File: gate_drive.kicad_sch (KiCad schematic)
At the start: 196 parts, among them J19 Conn_01x03, J20 Conn_01x03, Q1 Q_PNP_BEC, Q2 Q_PNP_BEC, Q3 Q_PNP_BEC, Q4 Q_PNP_BEC, Q5 Q_PNP_BEC, Q6 Q_PNP_BEC, U1 EG3113, U14 INA240A1D, U2 EG3113, U20 INA240A1D, U21 INA240A1D, U4 EG3113, U44 INA240A1D, U5 EG3113, U7 EG3113, U8 EG3113

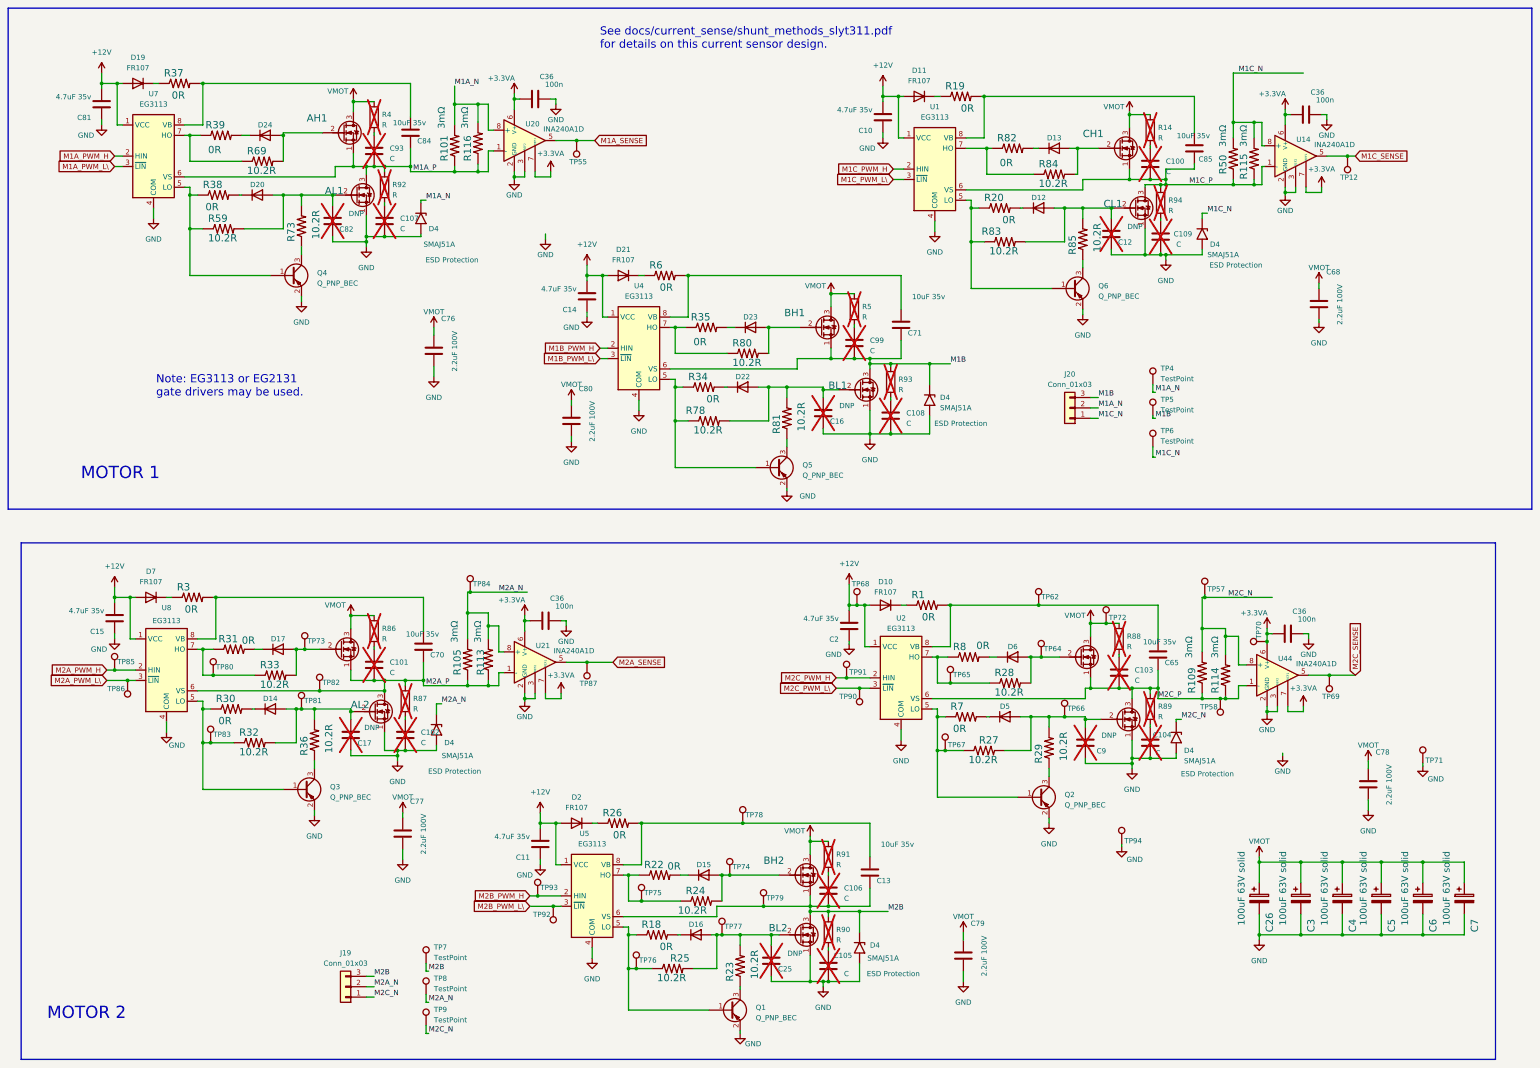
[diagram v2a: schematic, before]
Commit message: Updated board design ready for final design review before fabrication.
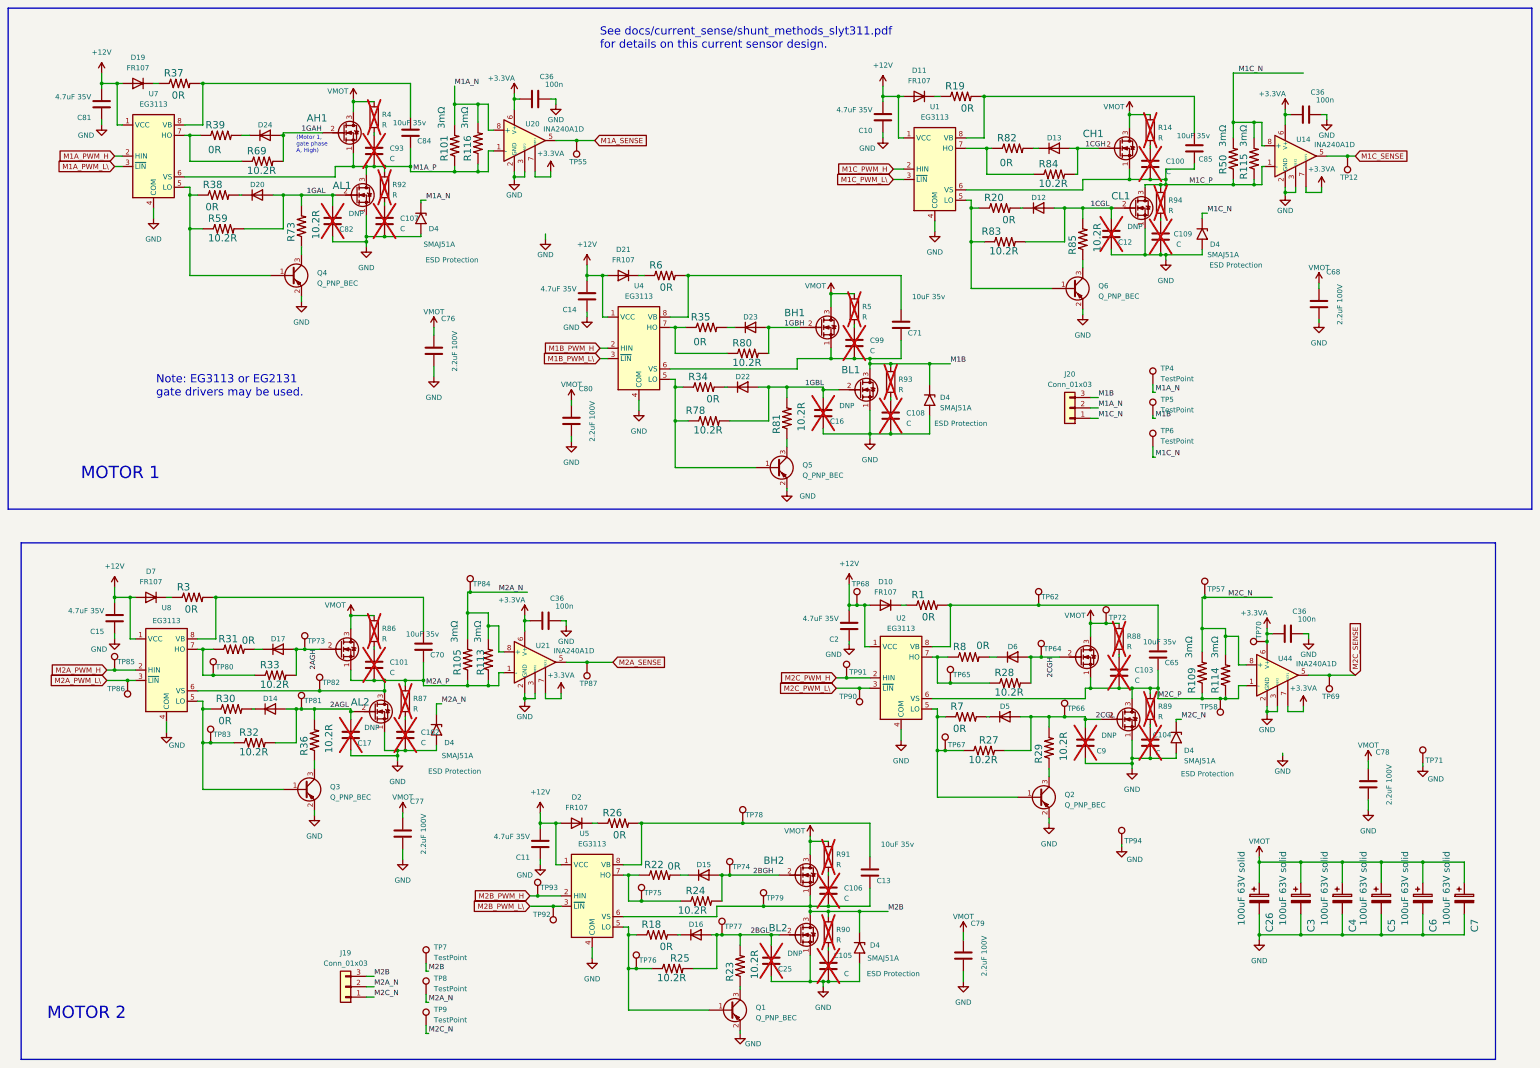
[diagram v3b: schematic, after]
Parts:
- C10, C11, C14, C15, C2, C81: value 4.7uF 35v -> 4.7uF 35V
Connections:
- net 1GAH: now reaches AH1.2 (G), D24.2 (A), R69.2
- net 2CGL: now reaches C9.2, CL2.2 (G), D5.2 (A), R27.2, R29.2, TP66.1
- net 2AGH: now reaches AH2.2 (G), D17.2 (A), R33.2, TP73.1
- net 1GBH: now reaches BH1.2 (G), D23.2 (A), R80.2
- net 2BGH: now reaches BH2.2 (G), D15.2 (A), R24.2, TP74.1
- net 1CGH: now reaches CH1.2 (G), D13.2 (A), R84.2
- net 2BGL: now reaches BL2.2 (G), C25.2, D16.2 (A), R23.2, R25.2, TP77.1
- net 1GBL: now reaches BL1.2 (G), C16.2, D22.2 (A), R78.2, R81.2
- net 1GAL: now reaches AL1.2 (G), C82.2, D20.2 (A), R59.2, R73.2
- net 2CGH: now reaches CH2.2 (G), D6.2 (A), R28.2, TP64.1
- net 2AGL: now reaches AL2.2 (G), C17.2, D14.2 (A), R32.2, R36.2, TP81.1
- net 1CGL: now reaches C12.2, CL1.2 (G), D12.2 (A), R83.2, R85.2
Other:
- note added: "(Motor 1, gate phase A, High)"
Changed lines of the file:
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@@
     (effects (font (size 2 2)) (justify left bottom))
   )
+  (text "(Motor 1,\ngate phase\nA, High)" (at 93.345 52.07 0)
+    (effects (font (size 1 1)) (justify left bottom))
+  )
   (text "MOTOR 1" (at 40.64 132.08 0)
     (effects (font (size 3 3)) (justify left bottom))
@@
     (effects (font (size 1.27 1.27)) (justify left bottom))
   )
+  (label "2BGL" (at 204.47 243.205 0) (fields_autoplaced)
+    (effects (font (size 1.27 1.27)) (justify left bottom))
+  )
   (label "M1C_P" (at 311.785 59.69 0) (fields_autoplaced)
     (effects (font (size 1.27 1.27)) (justify left bottom))
   )
+  (label "2AGL" (at 101.6 187.96 0) (fields_autoplaced)
+    (effects (font (size 1.27 1.27)) (justify left bottom))
+  )
   (label "M1C_N" (at 316.23 66.675 0) (fields_autoplaced)
     (effects (font (size 1.27 1.27)) (justify left bottom))
@@
     (effects (font (size 1.27 1.27)) (justify left bottom))
   )
+  (label "1GBL" (at 217.805 109.22 0) (fields_autoplaced)
+    (effects (font (size 1.27 1.27)) (justify left bottom))
+  )
+  (label "2AGH" (at 98.425 173.355 270) (fields_autoplaced)
+    (effects (font (size 1.27 1.27)) (justify right bottom))
+  )
   (label "M1A_N" (at 132.08 35.56 0) (fields_autoplaced)
     (effects (font (size 1.27 1.27)) (justify left bottom))
@@
     (effects (font (size 1.27 1.27)) (justify left bottom))
   )
+  (label "1GAL" (at 95.885 62.23 0) (fields_autoplaced)
+    (effects (font (size 1.27 1.27)) (justify left bottom))
+  )
+  (label "1CGH" (at 286.385 50.8 0) (fields_autoplaced)
+    (effects (font (size 1.27 1.27)) (justify left bottom))
+  )
   (label "M2C_N" (at 125.73 267.335 0) (fields_autoplaced)
     (effects (font (size 1.27 1.27)) (justify left bottom))
@@
     (effects (font (size 1.27 1.27)) (justify left bottom))
   )
+  (label "2CGH" (at 278.765 175.26 270) (fields_autoplaced)
+    (effects (font (size 1.27 1.27)) (justify right bottom))
+  )
   (label "M1A_N" (at 125.095 63.5 0) (fields_autoplaced)
     (effects (font (size 1.27 1.27)) (justify left bottom))
@@
     (effects (font (size 1.27 1.27)) (justify left bottom))
   )
+  (label "1GBH" (at 212.725 94.615 0) (fields_autoplaced)
+    (effects (font (size 1.27 1.27)) (justify left bottom))
+  )
   (label "M2A_P" (at 125.095 182.245 0) (fields_autoplaced)
     (effects (font (size 1.27 1.27)) (justify left bottom))
   )
+  (label "2BGH" (at 205.105 228.6 0) (fields_autoplaced)
+    (effects (font (size 1.27 1.27)) (justify left bottom))
+  )
+  (label "1GAH" (at 94.615 46.99 0) (fields_autoplaced)
+    (effects (font (size 1.27 1.27)) (justify left bottom))
+  )
   (label "M2C_N" (at 321.31 160.655 0) (fields_autoplaced)
     (effects (font (size 1.27 1.27)) (justify left bottom))
@@
     (effects (font (size 1.27 1.27)) (justify left bottom))
   )
+  (label "2CGL" (at 288.925 190.5 0) (fields_autoplaced)
+    (effects (font (size 1.27 1.27)) (justify left bottom))
+  )
+  (label "1CGL" (at 287.655 65.405 0) (fields_autoplaced)
+    (effects (font (size 1.27 1.27)) (justify left bottom))
+  )
   (label "M1C_N" (at 323.85 32.385 0) (fields_autoplaced)
     (effects (font (size 1.27 1.27)) (justify left bottom))
@@
       (effects (font (size 1.27 1.27)) (justify left bottom))
     )
-    (property "Value" "4.7uF 35v" (at 46.355 163.195 0)
+    (property "Value" "4.7uF 35V" (at 46.355 163.195 0)
       (effects (font (size 1.27 1.27)) (justify left bottom))
     )
@@
   (symbol (lib_id "Device:Q_NMOS_SGD") (at 231.14 109.855 0) (unit 1)
     (in_bom yes) (on_board yes) (dnp no)
-    (property "Reference" "BL1" (at 223.52 109.855 0)
+    (property "Reference" "BL1" (at 226.695 106.045 0)
       (effects (font (size 1.778 1.778)) (justify left bottom))
     )
@@
   (symbol (lib_id "Device:Q_NMOS_SGD") (at 107.95 62.23 0) (unit 1)
     (in_bom yes) (on_board yes) (dnp no)
-    (property "Reference" "AL1" (at 100.33 62.23 0)
+    (property "Reference" "AL1" (at 102.235 60.96 0)
       (effects (font (size 1.778 1.778)) (justify left bottom))
     )
@@
       (effects (font (size 1.27 1.27)) (justify left bottom))
     )
-    (property "Value" "4.7uF 35v" (at 161.925 84.455 0)
+    (property "Value" "4.7uF 35V" (at 161.925 84.455 0)
       (effects (font (size 1.27 1.27)) (justify left bottom))
     )
@@
       (effects (font (size 1.27 1.27)) (justify left bottom))
     )
-    (property "Value" "4.7uF 35v" (at 150.495 218.44 0)
+    (property "Value" "4.7uF 35V" (at 150.495 218.44 0)
       (effects (font (size 1.27 1.27)) (justify left bottom))
     )
@@
       (effects (font (size 1.27 1.27)) (justify left bottom))
     )
-    (property "Value" "4.7uF 35v" (at 43.18 37.465 0)
+    (property "Value" "4.7uF 35V" (at 43.18 37.465 0)
       (effects (font (size 1.27 1.27)) (justify left bottom))
     )
@@
   (symbol (lib_id "Device:Q_NMOS_SGD") (at 112.395 188.595 0) (unit 1)
     (in_bom yes) (on_board yes) (dnp no)
-    (property "Reference" "AL2" (at 106.68 187.96 0)
+    (property "Reference" "AL2" (at 106.68 187.325 0)
       (effects (font (size 1.778 1.778)) (justify left bottom))
     )
@@
       (effects (font (size 1.27 1.27)) (justify left bottom))
     )
-    (property "Value" "4.7uF 35v" (at 234.315 40.64 0)
+    (property "Value" "4.7uF 35V" (at 234.315 40.64 0)
       (effects (font (size 1.27 1.27)) (justify left bottom))
     )
@@
       (effects (font (size 1.27 1.27)) (justify left bottom))
     )
-    (property "Value" "4.7uF 35v" (at 226.06 165.1 0)
+    (property "Value" "4.7uF 35V" (at 226.06 165.1 0)
       (effects (font (size 1.27 1.27)) (justify left bottom))
     )
@@
   (symbol (lib_id "Device:Q_NMOS_SGD") (at 298.45 65.405 0) (unit 1)
     (in_bom yes) (on_board yes) (dnp no)
-    (property "Reference" "CL1" (at 290.83 65.405 0)
+    (property "Reference" "CL1" (at 292.735 63.5 0)
       (effects (font (size 1.778 1.778)) (justify left bottom))
     )

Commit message: Rev 3.1 updated files. ordered Nov 2 2023
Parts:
- J19, J20: LCSC C3040682 -> C99176; now in the parts list
- R23, R24, R25, R27, R28, R29, R32, R33, R36, R59, R69, R73, R78, R80, R81, R83, R84, R85: LCSC C22773 -> C2933129
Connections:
- net GND: now also Q1.3 (C), Q2.3 (C), Q3.3 (C), Q4.3 (C), Q5.3 (C), Q6.3 (C); no longer Q1.2 (E), Q2.2 (E), Q3.2 (E), Q4.2 (E), Q5.2 (E), Q6.2 (E)
- net at R23.1: now also Q1.2 (E); no longer Q1.3 (C)
- net at R29.1: now also Q2.2 (E); no longer Q2.3 (C)
- net at R81.1: now also Q5.2 (E); no longer Q5.3 (C)
- net at R36.1: now also Q3.2 (E); no longer Q3.3 (C)
- net at R85.1: now also Q6.2 (E); no longer Q6.3 (C)
- net at R73.1: now also Q4.2 (E); no longer Q4.3 (C)

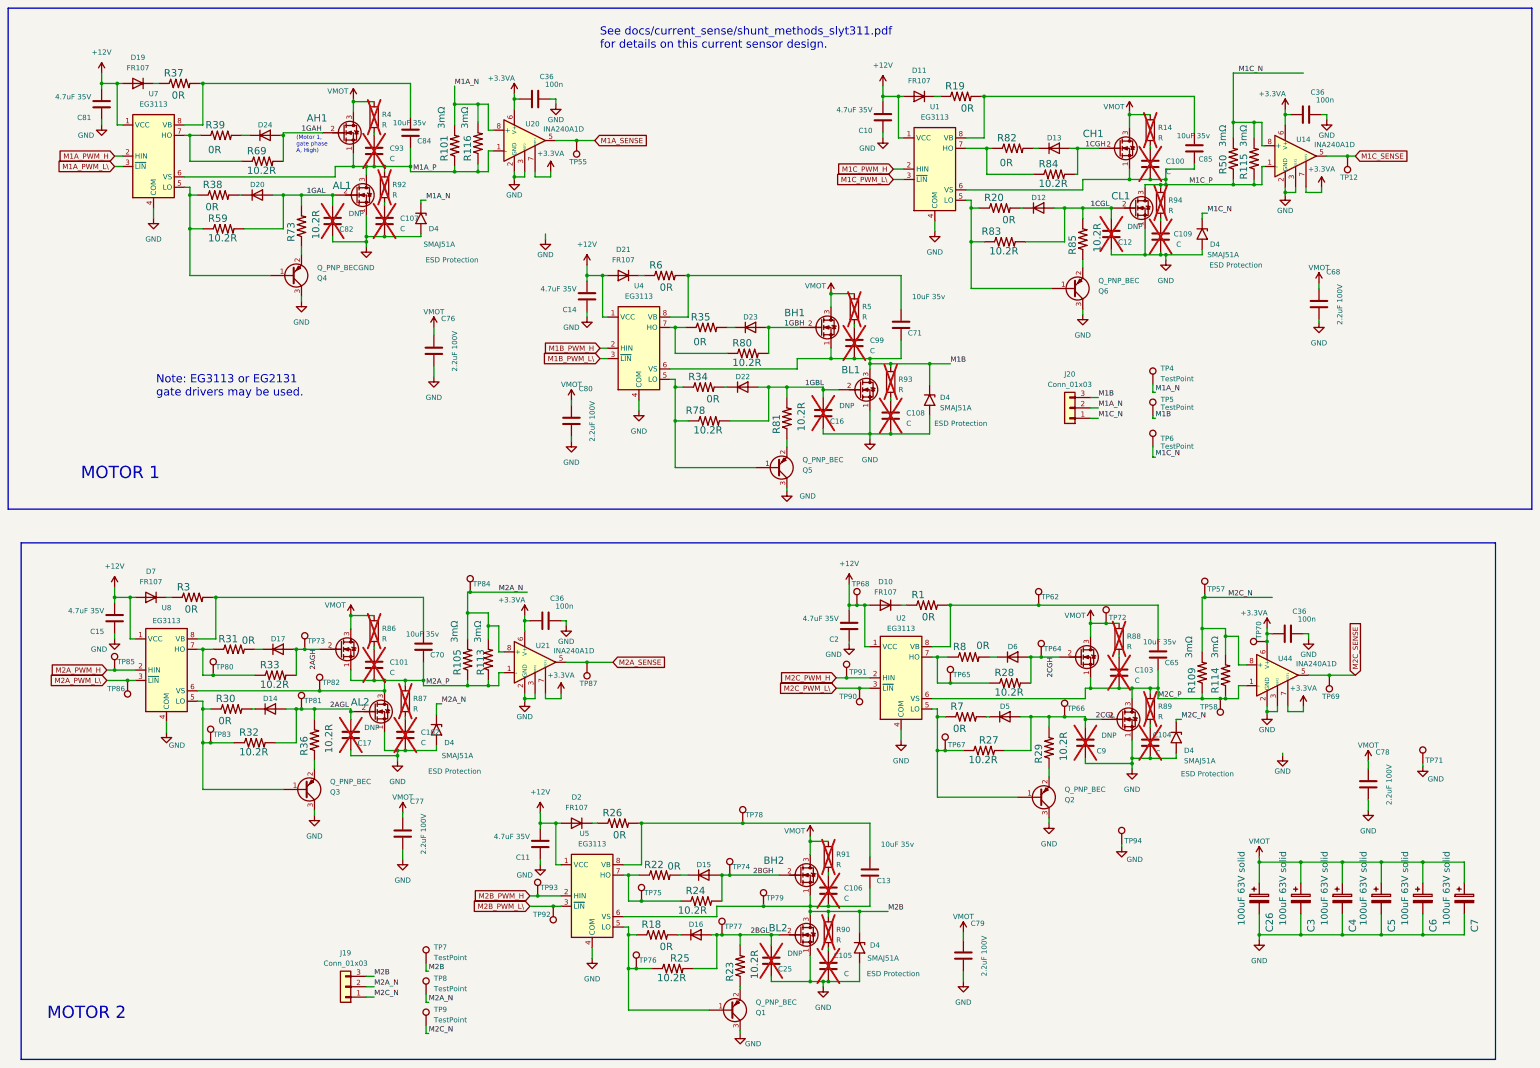
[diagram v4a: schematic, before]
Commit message: Update to Rev 3.2. Probably okay to order this rev.
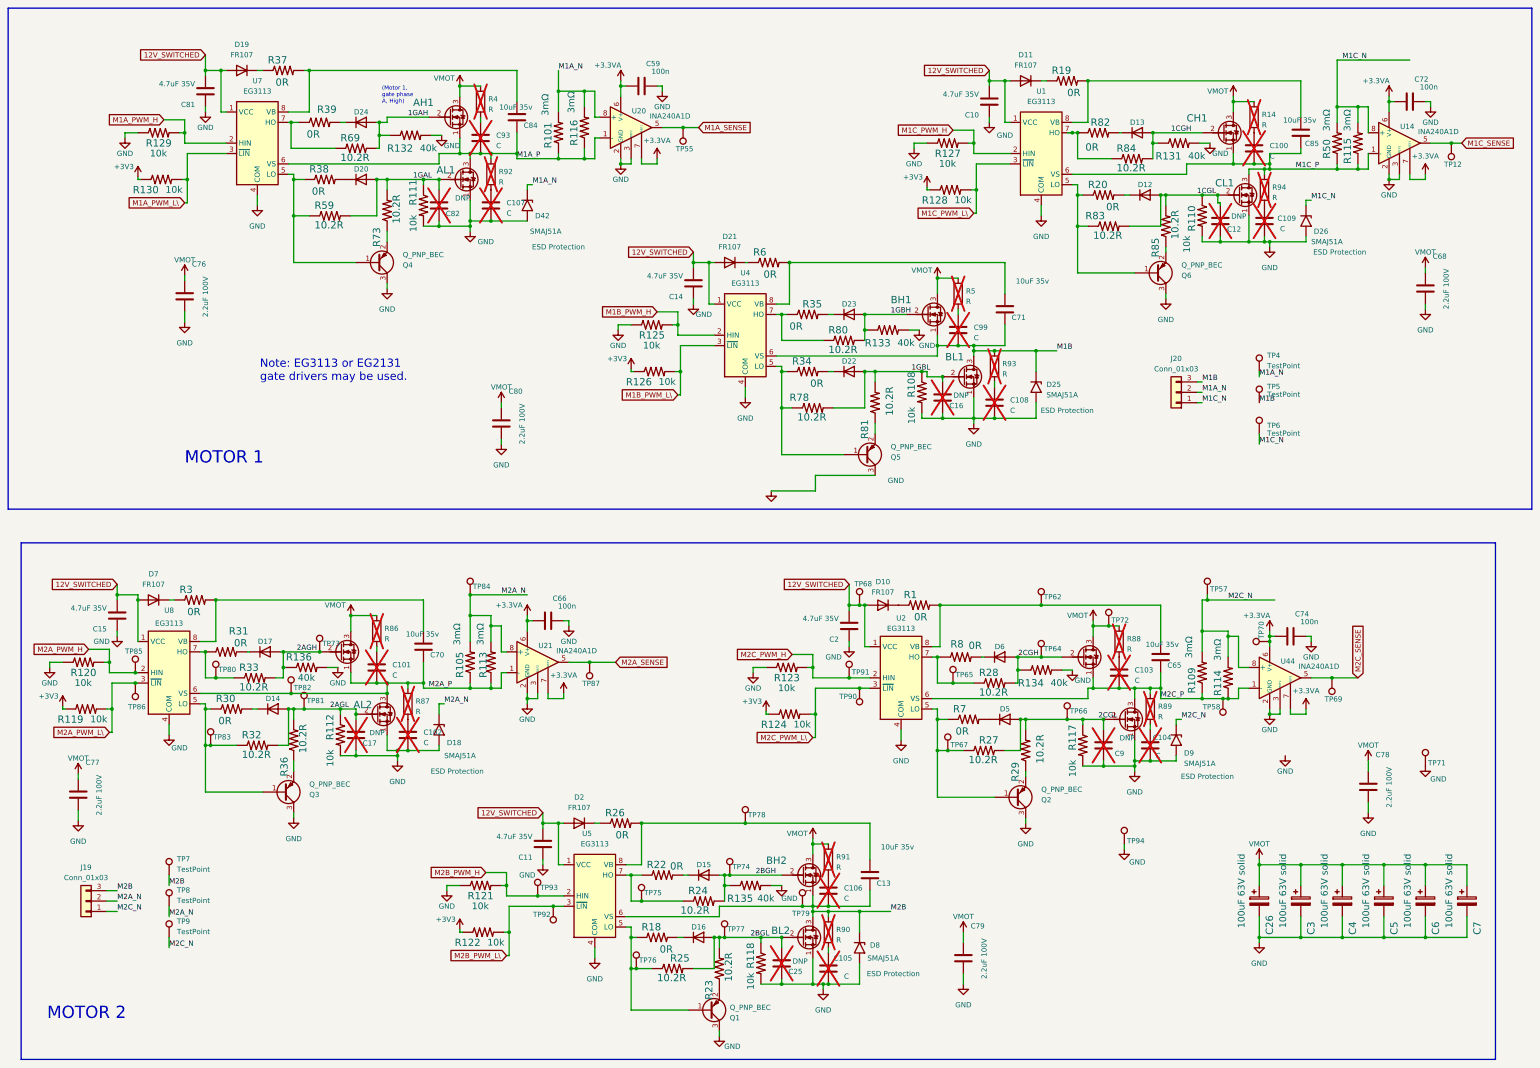
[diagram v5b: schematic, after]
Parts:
- added R108, R110, R111, R112, R117, R118, R119, R120, R121, R122, R123, R124, R125, R126, R127, R128, R129, R130: 10k, Resistor_SMD:R_0603_1608Metric, symbol MotorController:TAYLOR_RESISTOR
- added R131, R132, R133, R134, R135, R136: 40k, Resistor_SMD:R_0603_1608Metric, symbol MotorController:TAYLOR_RESISTOR
- renumbered C36 to C59, C36 to C66, C36 to C72, C36 to C74, D4 to D18, D4 to D25, D4 to D26, D4 to D42, D4 to D8, D4 to D9
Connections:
- net 1CGH: now also R131.1
- net 1CGL: now also R110.1
- net 1GAH: now also R132.1
- net 1GAL: now also R111.1
- net 1GBH: now also R133.1
- net 1GBL: now also R108.1
- net 2AGH: now also R136.1
- net 2AGL: now also R112.1
- net 2BGH: now also R135.1
- net 2BGL: now also R118.1
- net 2CGH: now also R134.1
- net 2CGL: now also R117.1
- net GND: now also R108.2, R110.2, R111.2, R112.2, R117.2, R118.2, R120.1, R121.1, R123.1, R125.1, R127.1, R129.1, R131.2, R132.2, R133.2, R134.2, R135.2, R136.2
- net M1A_PWM_H: now also R129.2
- net M1A_PWM_L\: now also R130.2
- net M1B_PWM_H: now also R125.2
- net M1B_PWM_L\: now also R126.2
- net M1C_PWM_H: now also R127.2
- net M1C_PWM_L\: now also R128.2
- net M2A_PWM_H: now also R120.2
- net M2A_PWM_L\: now also R119.2
- net M2B_PWM_H: now also R121.2
- net M2B_PWM_L\: now also R122.2
- net M2C_PWM_H: now also R123.2
- net M2C_PWM_L\: now also R124.2
- net +12V renamed 12V_SWITCHED
- new net +3V3: R119.1, R122.1, R124.1, R126.1, R128.1, R130.1
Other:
- note removed: "See docs/current_sense/shunt_methods_slyt311.pdf for details on this current sensor design."
- moved on the sheet: AH1, AL1, AL2, BH1, BH2, BL1, BL2, C10, C100, C101, C102, C104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
